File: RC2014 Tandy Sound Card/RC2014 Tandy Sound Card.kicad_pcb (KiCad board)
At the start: 2 copper layers, 99.1 x 49.5 mm, 8 parts, among them J1 CONN_01X39, J2 Sound, U1 74LS138, U2 74LS245, U3 SN76489AN

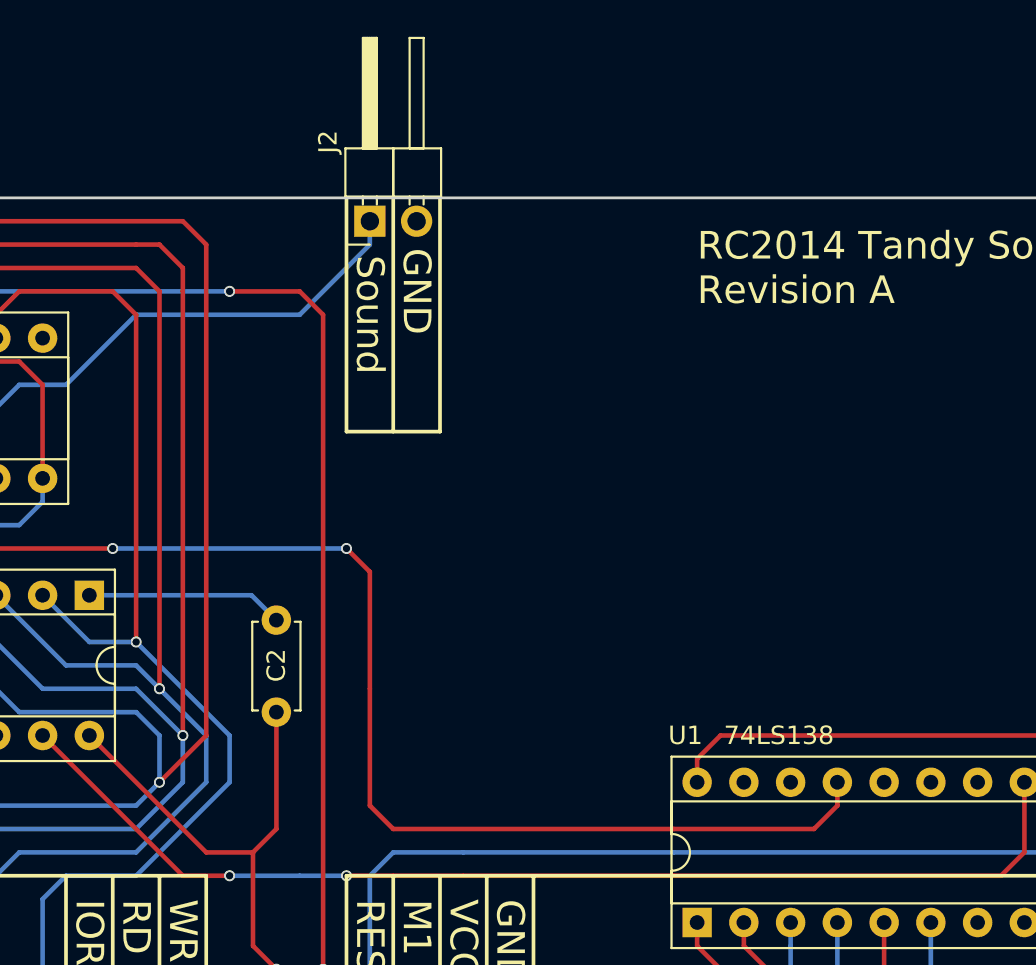
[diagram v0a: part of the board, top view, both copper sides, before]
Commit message: Added TDA7065A audio amplification
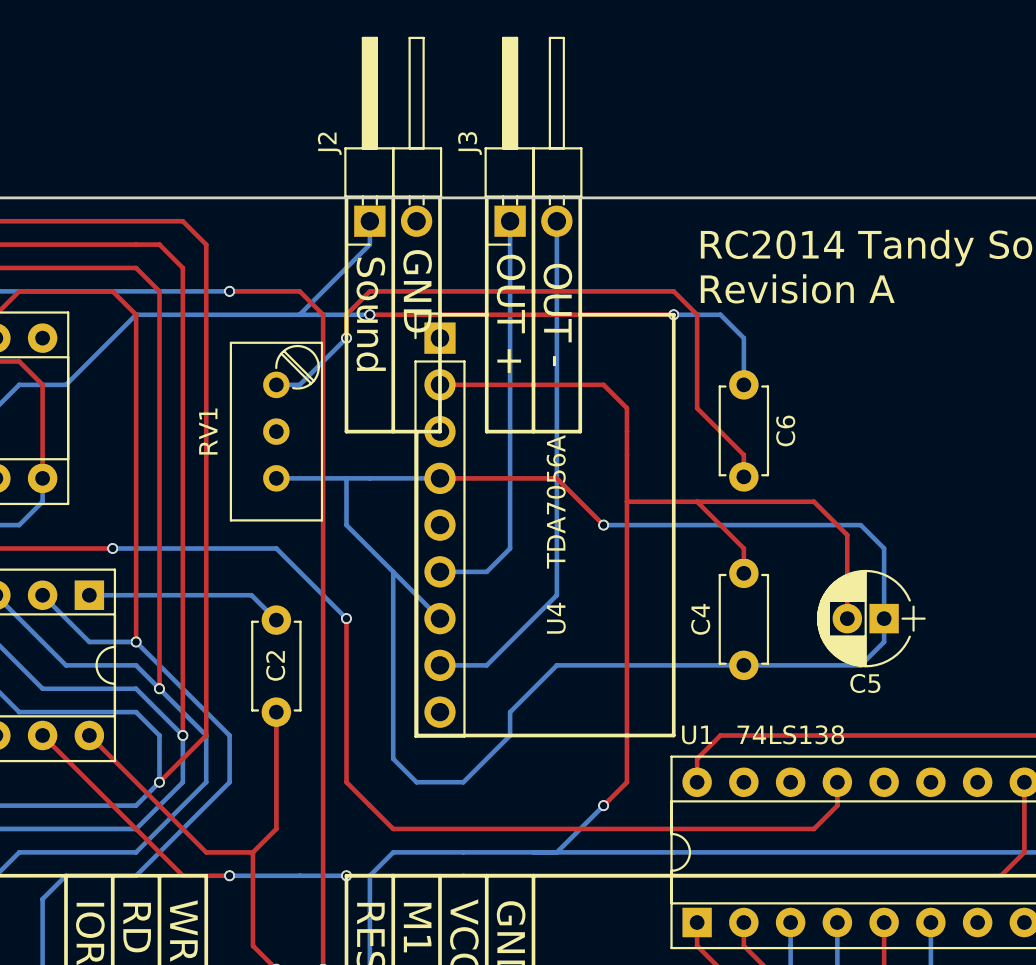
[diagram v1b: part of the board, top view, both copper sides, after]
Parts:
- added C4: 470nF, Capacitors_THT:C_Disc_D4.7mm_W2.5mm_P5.00mm, F.Cu at (186.7, 110.5)
- added C5: 220uF, Capacitors_THT:CP_Radial_D5.0mm_P2.00mm, F.Cu at (194.3, 108.0)
- added C6: 470nF, Capacitors_THT:C_Disc_D4.7mm_W2.5mm_P5.00mm, F.Cu at (186.7, 95.2)
- added J3: Speaker Out, Pin_Headers:Pin_Header_Angled_1x02_Pitch2.54mm, F.Cu at (174.0, 86.4)
- added RV1: 10k, Potentiometers:Potentiometer_Trimmer_Bourns_3296W, F.Cu at (161.3, 95.2)
- added U4: TDA7056A, Pin_Headers:Pin_Header_Straight_1x09_Pitch2.54mm, F.Cu at (170.2, 92.7)
- J2: value Sound -> Line Out
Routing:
- net GND: track 103.1 -> 193.8 mm, vias 1 -> 2
- net VCC: track 128.0 -> 187.9 mm, vias 3 -> 4
- net Net-(C6-Pad2): track 0.00 -> 36.1 mm, vias 0 -> 1
- net SPKR_OUT-: track 0.00 -> 28.2 mm
- net SND_OUT: track 29.1 -> 56.3 mm, vias 0 -> 2
- net SPKR_OUT+: track 0.00 -> 22.1 mm
- net PORT32_WR: track 69.4 -> 67.2 mm
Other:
- board text added: "OUT +"
- board text added: "OUT -"

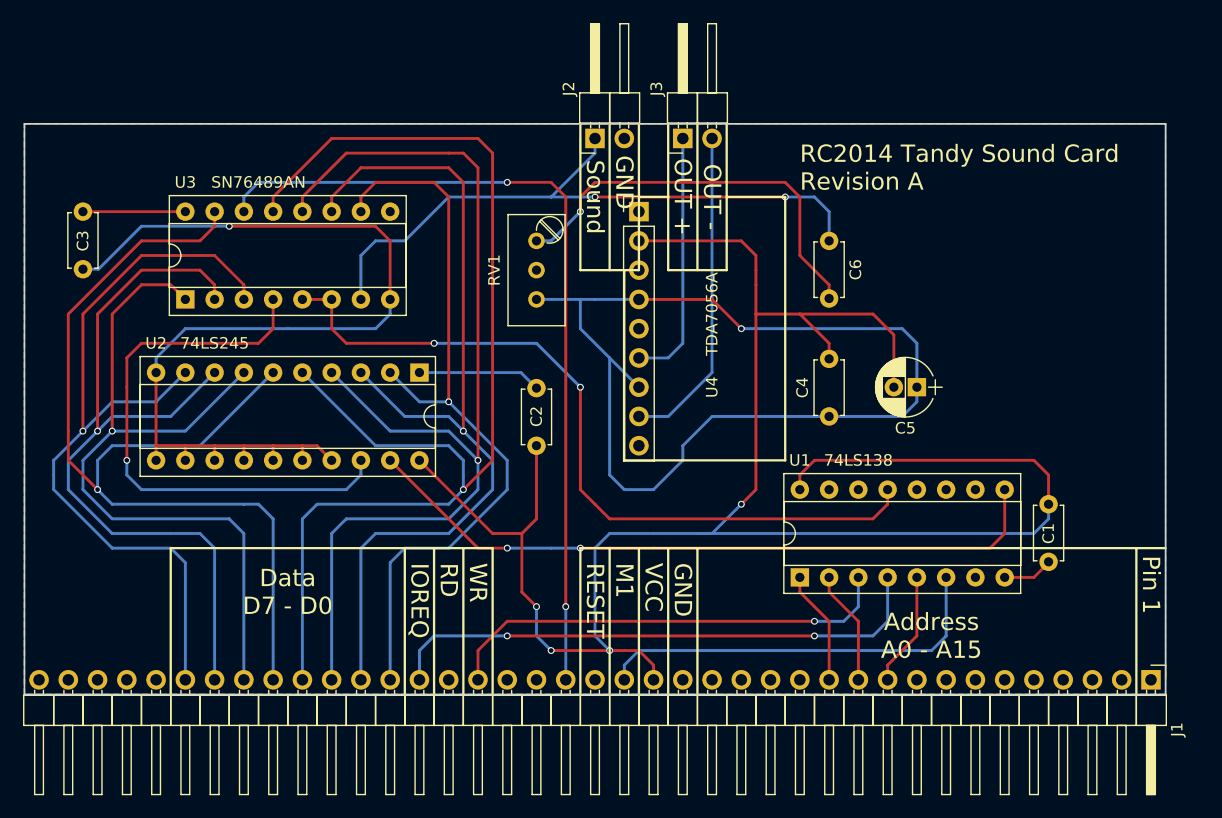
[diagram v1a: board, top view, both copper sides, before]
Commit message: Added pinheaders for selecting address
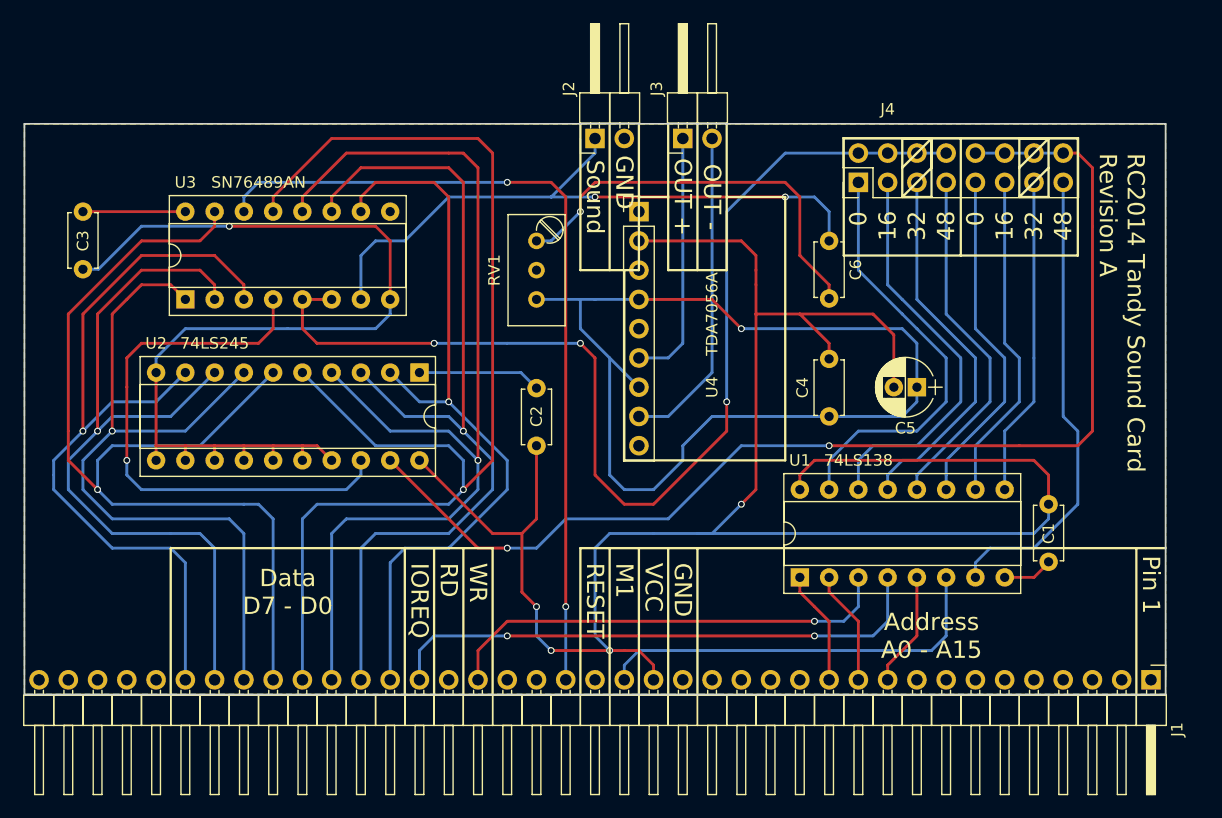
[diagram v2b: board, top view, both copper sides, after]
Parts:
- added J4: CONN_02X08, Pin_Headers:Pin_Header_Straight_2x08_Pitch2.54mm, F.Cu at (189.2, 90.2)
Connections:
- U1 pad 10: (no net) -> Net-(J4-Pad11)
- U1 pad 11: (no net) -> Net-(J4-Pad9)
- U1 pad 12: (no net) -> Net-(J4-Pad7)
- U1 pad 13: PORT32_WR -> Net-(J4-Pad5)
- U1 pad 14: (no net) -> Net-(J4-Pad3)
- U1 pad 15: (no net) -> Net-(J4-Pad1)
- U1 pad 7: (no net) -> Net-(J4-Pad15)
- U1 pad 9: PORT32_RD -> Net-(J4-Pad13)
- U2 pad 19: PORT32_RD -> IO_RD
- U3 pad 5: PORT32_WR -> IO_WR
- U3 pad 6: PORT32_WR -> IO_WR
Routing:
- net IO_RD: track 0.00 -> 101.9 mm, vias 0 -> 2
- net IO_WR: track 0.00 -> 97.0 mm, vias 0 -> 3
- net PORT32_WR: track 67.2 -> 0.00 mm, vias 2 -> 0
- net PORT32_RD: track 60.8 -> 0.00 mm, vias 2 -> 0
- net Net-(J4-Pad15): track 0.00 -> 40.7 mm
- net Net-(J4-Pad1): track 0.00 -> 37.0 mm
- net Net-(J4-Pad3): track 0.00 -> 35.2 mm
- net Net-(J4-Pad5): track 0.00 -> 32.7 mm
- net Net-(J4-Pad7): track 0.00 -> 30.9 mm
- net Net-(J4-Pad9): track 0.00 -> 29.8 mm
- net Net-(J4-Pad11): track 0.00 -> 28.8 mm
- net Net-(J4-Pad13): track 0.00 -> 27.7 mm
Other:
- board text added: "0"
- board text added: "16"
- board text added: "32"
- board text added: "48"

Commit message: Tandy Sound card revision A
PCB layout done including silkscreen. Includes TDA7056A mono amplifier circuit.
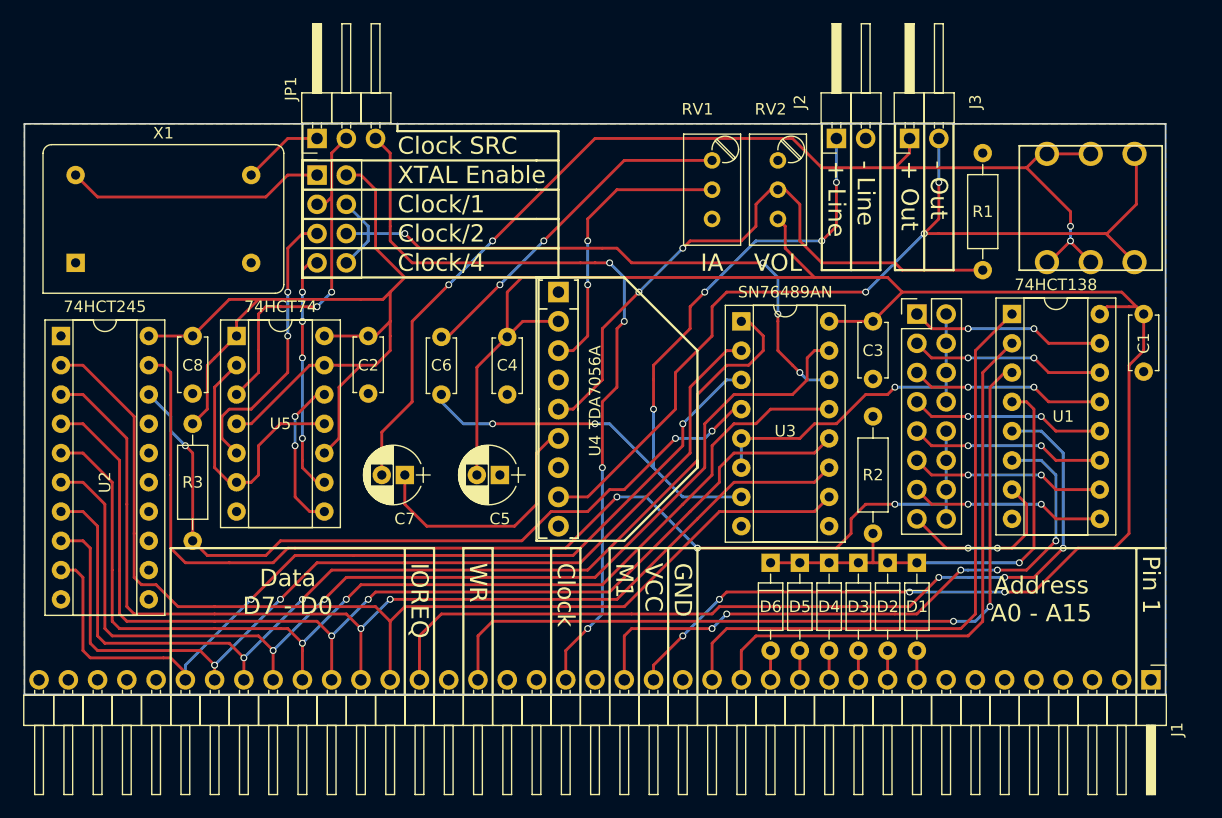
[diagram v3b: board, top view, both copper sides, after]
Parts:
- added C7: 470uF, Capacitors_THT:CP_Radial_D5.0mm_P2.00mm, F.Cu at (149.9, 115.6)
- added C8: 100nF, Capacitors_THT:C_Disc_D4.7mm_W2.5mm_P5.00mm, F.Cu at (131.4, 103.5)
- added D1: 1N4848, Diodes_THT:D_DO-35_SOD27_P7.62mm_Horizontal, F.Cu at (194.3, 123.2)
- added D2: 1N4848, Diodes_THT:D_DO-35_SOD27_P7.62mm_Horizontal, F.Cu at (191.8, 123.2)
- added D3: 1N4848, Diodes_THT:D_DO-35_SOD27_P7.62mm_Horizontal, F.Cu at (189.2, 123.2)
- added D4: 1N4848, Diodes_THT:D_DO-35_SOD27_P7.62mm_Horizontal, F.Cu at (186.7, 123.2)
- added D5: 1N4848, Diodes_THT:D_DO-35_SOD27_P7.62mm_Horizontal, F.Cu at (184.2, 123.2)
- added D6: 1N4848, Diodes_THT:D_DO-35_SOD27_P7.62mm_Horizontal, F.Cu at (181.6, 123.2)
- added J5: JACK_TRS_6PINS, rc2014:cliff_fcr1295_socket, F.Cu at (203.2, 87.0)
- added J6: CONN_02X04, Pin_Headers:Pin_Header_Straight_2x04_Pitch2.54mm, F.Cu at (142.2, 89.5)
- added JP1: Clock source, Pin_Headers:Pin_Header_Angled_1x03_Pitch2.54mm, F.Cu at (142.2, 86.4)
- added R1: 1k, Resistors_THT:R_Axial_DIN0207_L6.3mm_D2.5mm_P10.16mm_Horizontal, F.Cu at (200.0, 97.8)
- added R2: 10k, Resistors_THT:R_Axial_DIN0207_L6.3mm_D2.5mm_P10.16mm_Horizontal, F.Cu at (190.5, 120.7)
- added R3: 10k, Resistors_THT:R_Axial_DIN0207_L6.3mm_D2.5mm_P10.16mm_Horizontal, F.Cu at (131.4, 111.1)
- added RV2: 10k, Potentiometers:Potentiometer_Trimmer_Bourns_3296W, F.Cu at (182.2, 88.3)
- added U5: 74HCT74, Housings_DIP:DIP-14_W7.62mm_Socket, F.Cu at (135.3, 103.5)
- added X1: 1MHz, Oscillators:Oscillator_DIP-14, F.Cu at (121.3, 97.2)
- C4: value 470nF -> 100nF
- U1: value 74LS138 -> 74HCT138
- U2: value 74LS245 -> 74HCT245
- U4: footprint Pin_Headers:Pin_Header_Straight_1x09_Pitch2.54mm -> Housings_SIP:SIP9_Housing
- moved C3 69.2 mm to (190.5, 102.2)
- moved U3 48.3 mm to (179.1, 102.2), turned to 0 degrees
- moved C5 37.0 mm to (158.1, 115.6)
- moved C6 36.2 mm to (153.0, 108.6), turned to 90 degrees
- moved U2 31.3 mm to (120.0, 103.5), turned to 0 degrees
- moved U1 29.4 mm to (202.6, 101.6), turned to 0 degrees
- moved C4 28.0 mm to (158.8, 108.6)
- moved J2 21.0 mm to (187.3, 86.4)
- moved J3 19.7 mm to (193.7, 86.4)
- moved U4 18.5 mm to (163.2, 109.9), turned to 270 degrees
- moved C1 18.5 mm to (214.0, 101.6)
- moved C2 17.4 mm to (146.7, 103.5), turned to 270 degrees
- moved RV1 16.8 mm to (176.5, 88.3)
- moved J4 12.5 mm to (194.3, 101.6), turned to 0 degrees
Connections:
- net Net-(J4-Pad1) renamed /WR_Port_0
- net Net-(J4-Pad11) renamed /RD_Port_1
- net Net-(J4-Pad13) renamed /RD_Port_2
- net Net-(J4-Pad15) renamed /RD_Port_3
- net Net-(J4-Pad3) renamed /WR_Port_1
- net Net-(J4-Pad5) renamed /WR_Port_2
- net Net-(J4-Pad7) renamed /WR_Port_3
- net Net-(J4-Pad9) renamed /RD_Port_0
- J1 pad 13: (no net) -> A3
- J1 pad 14: (no net) -> A2
- J1 pad 15: (no net) -> A1
- J1 pad 16: (no net) -> A0
- J1 pad 9: (no net) -> A7
- J3 pad 1: SPKR_OUT+ -> Net-(C7-Pad2)
- U1 pad 1: A4 -> A0
- U1 pad 2: A5 -> A1
- U1 pad 4: IOREQ -> Net-(D1-Pad1)
- U1 pad 5: A6 -> IOREQ
- U3 pad 14: CLOCK -> SND_CLOCK
- U4 pad 5: (no net) -> Net-(R1-Pad1)
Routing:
- net GND: track 193.8 -> 0.00 mm, vias 2 -> 0
- net Net-(C7-Pad2): track 0.00 -> 99.1 mm, vias 0 -> 4
- net VCC: track 187.9 -> 258.8 mm
- net IO_WR: track 97.0 -> 29.8 mm, vias 3 -> 1
- net SND_CLOCK: track 0.00 -> 57.5 mm, vias 0 -> 4
- net A0: track 0.00 -> 54.4 mm
- net Net-(R1-Pad1): track 0.00 -> 53.2 mm, vias 0 -> 2
- net SPKR_OUT-: track 28.2 -> 80.9 mm, vias 0 -> 3
- net A1: track 0.00 -> 49.7 mm
- net Net-(D1-Pad1): track 0.00 -> 40.2 mm, vias 0 -> 1
- net WR: track 39.7 -> 70.8 mm, vias 1 -> 2
- net CLOCK/1: track 0.00 -> 30.3 mm, vias 0 -> 2
- net IOREQ: track 48.0 -> 76.3 mm, vias 2 -> 3
- net D0: track 66.5 -> 93.6 mm, vias 1 -> 0
- net D5: track 66.0 -> 91.8 mm, vias 1 -> 2
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- removed copper zone on F.Cu, net VCC
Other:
- board text added: "+ Line"
- board text added: "+ Out"
- board text added: "- Line"
- board text added: "- Out"
- board text added: "1"
- board text added: "2"
- board text added: "3"
- board text added: "Clock"
- board text added: "Clock SRC"
- board text added: "Clock/1"
- board text added: "Clock/2"
- board text added: "Clock/4"
- board text added: "IA"
- board text added: "System"
- board text added: "VOL"
- board text added: "XTAL"
- board text added: "XTAL Enable"
- board text removed: "16"
- board text removed: "32"
- board text removed: "48"
- board text removed: "OUT +"
- board text removed: "OUT -"
- board text removed: "RESET"
- board text removed: "Sound"
